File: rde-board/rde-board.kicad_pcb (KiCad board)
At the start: 2 copper layers, 56 x 65 mm, 21 parts, among them J1 RPI conn, J2 Mouse / Joy 1, J3 Joy 2, U1 ULN2003A, U2 ULN2003A

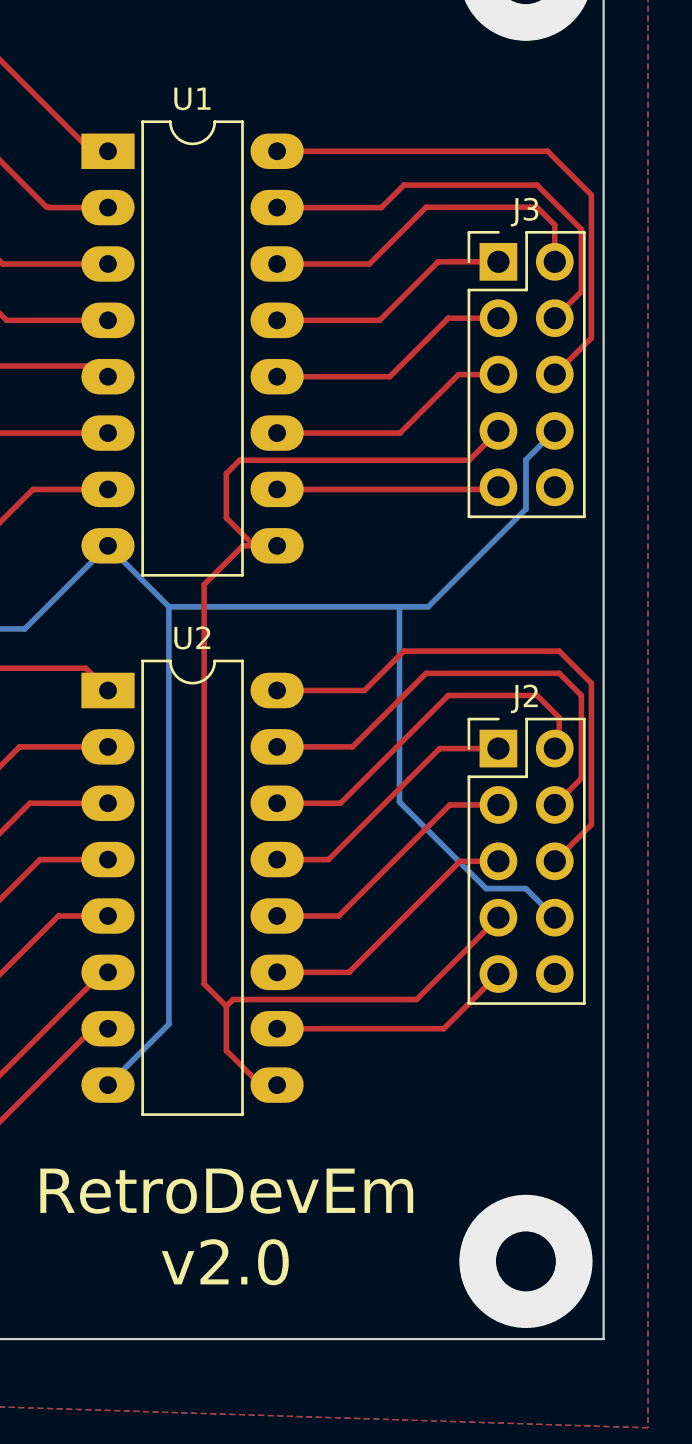
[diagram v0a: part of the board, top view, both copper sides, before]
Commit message: Fix ports connectors routing on board v2.1
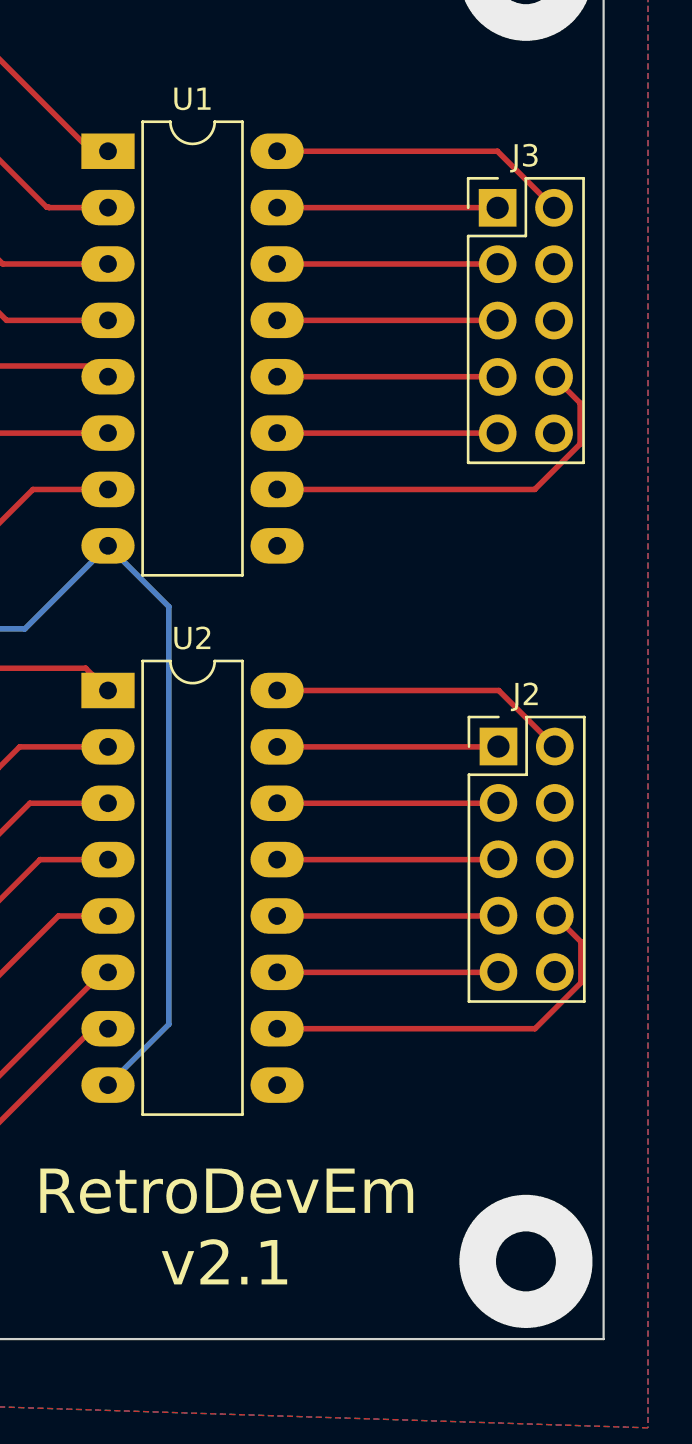
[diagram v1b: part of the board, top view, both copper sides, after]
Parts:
- moved J3 2.43 mm to (151.2, 64.0)
- moved J2 0.09 mm to (151.3, 88.3)
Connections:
- J2 pad 4: Net-(J2-Pad4) -> unconnected-(J2-Pad4)
- J2 pad 6: Net-(J2-Pad6) -> GND
- J2 pad 7: /+5V -> Net-(J2-Pad7)
- J2 pad 8: GND -> Net-(J2-Pad8)
- J3 pad 4: Net-(J3-Pad4) -> unconnected-(J3-Pad4)
- J3 pad 6: Net-(J3-Pad6) -> GND
- J3 pad 7: /+5V -> Net-(J3-Pad7)
- J3 pad 8: GND -> Net-(J3-Pad8)
- U1 pad 10: Net-(J3-Pad9) -> Net-(J3-Pad8)
- U1 pad 11: Net-(J3-Pad5) -> Net-(J3-Pad9)
- U1 pad 12: Net-(J3-Pad3) -> Net-(J3-Pad7)
- U1 pad 13: Net-(J3-Pad1) -> Net-(J3-Pad5)
- U1 pad 14: Net-(J3-Pad2) -> Net-(J3-Pad3)
- U1 pad 15: Net-(J3-Pad4) -> Net-(J3-Pad1)
- U1 pad 16: Net-(J3-Pad6) -> Net-(J3-Pad2)
- U1 pad 9: /+5V -> unconnected-(U1-Pad9)
- U2 pad 10: Net-(J2-Pad9) -> Net-(J2-Pad8)
- U2 pad 11: Net-(J2-Pad5) -> Net-(J2-Pad9)
- U2 pad 12: Net-(J2-Pad3) -> Net-(J2-Pad7)
- U2 pad 13: Net-(J2-Pad1) -> Net-(J2-Pad5)
- U2 pad 14: Net-(J2-Pad2) -> Net-(J2-Pad3)
- U2 pad 15: Net-(J2-Pad4) -> Net-(J2-Pad1)
- U2 pad 16: Net-(J2-Pad6) -> Net-(J2-Pad2)
- U2 pad 9: /+5V -> unconnected-(U2-Pad9)
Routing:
- net /+5V: track 60.1 -> 0.00 mm
- net GND: track 150.3 -> 110.4 mm
- net Net-(J2-Pad6): track 24.2 -> 0.00 mm
- net Net-(J3-Pad6): track 23.8 -> 0.00 mm
- net Net-(J2-Pad4): track 20.9 -> 0.00 mm
- net Net-(J3-Pad4): track 19.5 -> 0.00 mm
- net Net-(J2-Pad8): track 0.00 -> 18.1 mm
- net Net-(J3-Pad8): track 0.00 -> 18.0 mm
- net Net-(J2-Pad7): track 0.00 -> 9.98 mm
- net Net-(J3-Pad7): track 0.00 -> 9.94 mm
- net Net-(J2-Pad2): track 16.6 -> 13.6 mm
- net Net-(J2-Pad5): track 12.0 -> 9.98 mm
- net Net-(J2-Pad3): track 12.0 -> 9.98 mm
- net Net-(J2-Pad1): track 12.0 -> 9.98 mm
- net Net-(J3-Pad2): track 15.6 -> 13.5 mm
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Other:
- board text added: "RetroDevEm v2.1"
- board text removed: "RetroDevEm v2.0"
